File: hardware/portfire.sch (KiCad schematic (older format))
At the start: 56 parts, among them IC101 STM32F407VGT6TR, IC102 TPS62152, IC103 25AA02E48, IC104 ADP3335, IC105 SNx5176B, P101 SWD_TC, P102 AUX_BUS_RX, P103 AUX_BUS_RX, X101 PART, X102 PART, X103 PART, X104 PART, Y101 26M

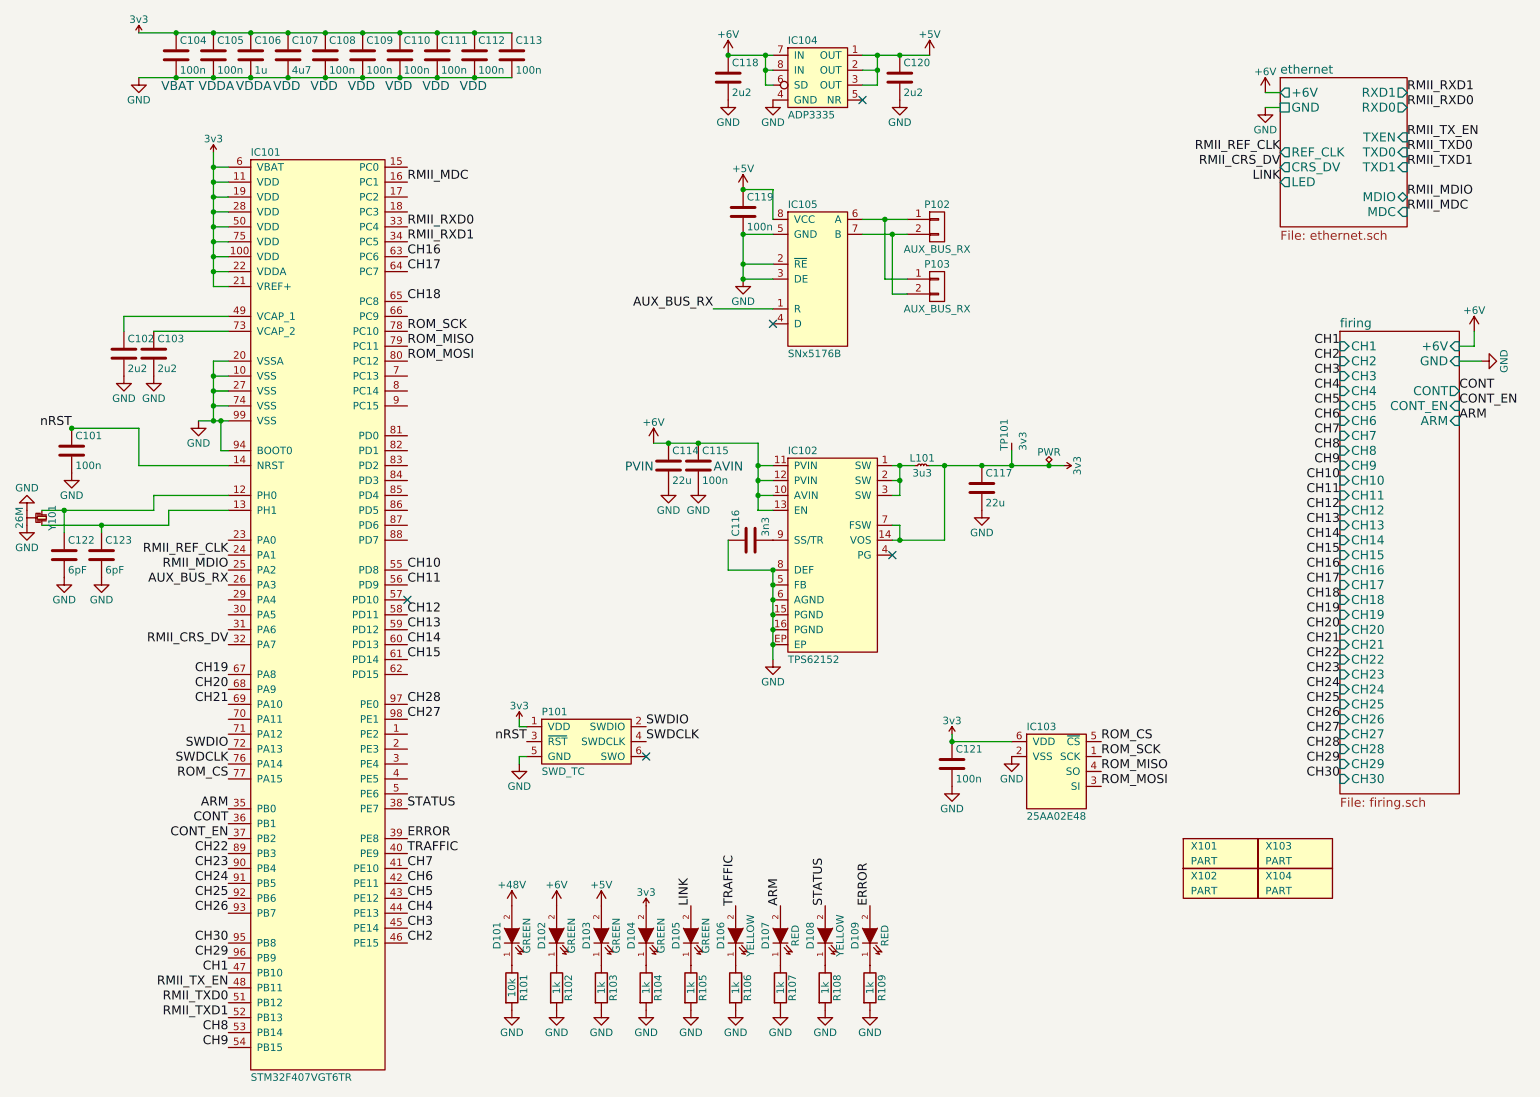
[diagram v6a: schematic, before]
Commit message: Fixed ERC and DRC issues
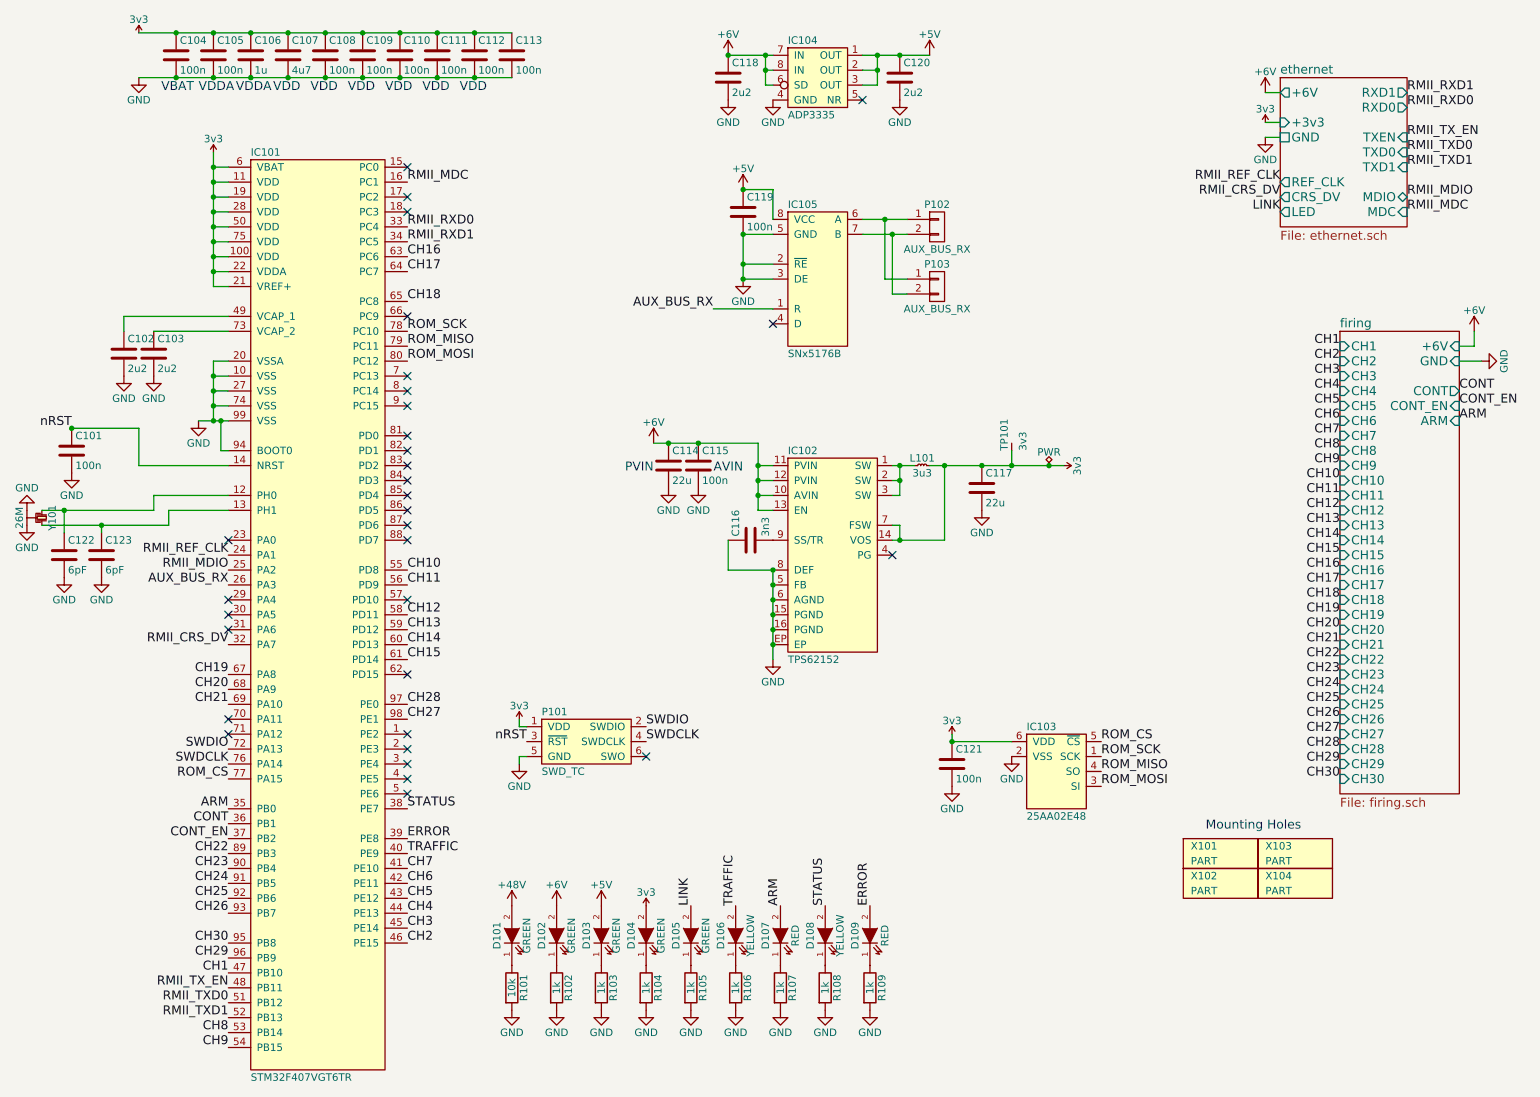
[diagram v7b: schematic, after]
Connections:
- no-connect marks 5 -> 32
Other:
- note added: "Mounting Holes"
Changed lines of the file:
@@
 F3 "RXD1" O R 10200 1050 60
 F4 "RXD0" O R 10200 1150 60
-F5 "CRS_DV" O L 9350 1550 60
-F6 "REF_CLK" O L 9350 1450 60
+F5 "CRS_DV" O L 9350 1750 60
+F6 "REF_CLK" O L 9350 1650 60
 F7 "TXEN" I R 10200 1350 60
 F8 "TXD0" I R 10200 1450 60
@@
 F10 "MDIO" B R 10200 1750 60
 F11 "MDC" I R 10200 1850 60
-F12 "LED" O L 9350 1650 60
-F13 "GND" U L 9350 1150 60
+F12 "LED" O L 9350 1850 60
+F13 "GND" U L 9350 1350 60
+F14 "+3v3" I L 9350 1250 60
 $EndSheet
 Text Label 2300 4150 2    60   ~ 0
 RMII_REF_CLK
-Text Label 9350 1450 2    60   ~ 0
+Text Label 9350 1650 2    60   ~ 0
 RMII_REF_CLK
 Text Label 2300 4250 2    60   ~ 0
@@
 Text Label 2300 4750 2    60   ~ 0
 RMII_CRS_DV
-Text Label 9350 1550 2    60   ~ 0
+Text Label 9350 1750 2    60   ~ 0
 RMII_CRS_DV
 Text Label 2300 7050 2    60   ~ 0
@@
 L GND #PWR02
 U 1 1 57F2FF50
-P 9250 1150
-F 0 "#PWR02" H 9250 900 50  0001 C CNN
-F 1 "GND" H 9250 1000 50  0000 C CNN
-F 2 "" H 9250 1150 50  0000 C CNN
-F 3 "" H 9250 1150 50  0000 C CNN
-	1    9250 1150
-	1    0    0    -1
-$EndComp
-Wire Wire Line
-	9250 1150 9350 1150
+P 9250 1350
+F 0 "#PWR02" H 9250 1100 50  0001 C CNN
+F 1 "GND" H 9250 1200 50  0000 C CNN
+F 2 "" H 9250 1350 50  0000 C CNN
+F 3 "" H 9250 1350 50  0000 C CNN
+	1    9250 1350
+	1    0    0    -1
+$EndComp
 $Comp
 L +6V #PWR03
@@
 Text Label 3500 6050 0    60   ~ 0
 ERROR
-Text Label 9350 1650 2    60   ~ 0
+Text Label 9350 1850 2    60   ~ 0
 LINK
 $Comp
@@
 Text Label 2300 6150 2    60   ~ 0
 CH22
+NoConn ~ 3500 1550
+NoConn ~ 3500 1750
+NoConn ~ 3500 1850
+NoConn ~ 3500 2550
+NoConn ~ 3500 2950
+NoConn ~ 3500 3050
+NoConn ~ 3500 3150
+NoConn ~ 3500 3350
+NoConn ~ 3500 3450
+NoConn ~ 3500 3550
+NoConn ~ 3500 3650
+NoConn ~ 3500 3750
+NoConn ~ 3500 3850
+NoConn ~ 3500 3950
+NoConn ~ 3500 4050
+NoConn ~ 2300 4050
+NoConn ~ 2300 4450
+NoConn ~ 2300 4550
+NoConn ~ 2300 4650
+NoConn ~ 3500 4950
+NoConn ~ 3500 5350
+NoConn ~ 3500 5450
+NoConn ~ 3500 5550
+NoConn ~ 3500 5650
+NoConn ~ 3500 5750
+NoConn ~ 2300 5250
+NoConn ~ 2300 5350
+Text Notes 8850 6000 0    60   ~ 0
+Mounting Holes
+Wire Wire Line
+	9250 1350 9350 1350
+$Comp
+L 3v3 #PWR048
+U 1 1 58012D29
+P 9250 1250
+F 0 "#PWR048" H 9250 1360 50  0001 L CNN
+F 1 "3v3" H 9250 1340 50  0000 C CNN
+F 2 "" H 9250 1250 60  0001 C CNN
+F 3 "" H 9250 1250 60  0001 C CNN
+	1    9250 1250
+	1    0    0    -1
+$EndComp
+Wire Wire Line
+	9350 1250 9250 1250
 $EndSCHEMATC
